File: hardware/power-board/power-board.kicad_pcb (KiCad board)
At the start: 2 copper layers, 197 x 65 mm, 25 parts, among them J1 SW_SPST, J2 Main Board, J3 DMX512 Out Jack, J4 DMX512, K1 SPST-NO, K2 SPST-NO, P1 IEC320-C14, P2 IEC320-C13, P3 IEC320-C13, U1 NUD3112DMT1G, U2 MAX3075E

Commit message: Updated PCB layout, still refining things
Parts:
- added LOGO: G***, lib_fp:Dektronics-logo, F.Cu at (94.0, 96.5)
- moved J2 58.4 mm to (156.0, 99.8)
- moved U1 37.9 mm to (142.2, 97.8)
- moved C1 23.1 mm to (209.6, 99.6), turned to -90 degrees
- moved NT1 15.0 mm to (220.0, 100.0), turned to 180 degrees
- moved D1 8.89 mm to (193.5, 99.6), turned to -90 degrees
- moved C2 8.13 mm to (201.9, 99.6), turned to -90 degrees
- moved U2 6.95 mm to (52.5, 76.5)
- moved C3 6.90 mm to (48.5, 72.9)
- moved TP1 6.16 mm to (175.5, 96.1)
- moved R1 4.83 mm to (52.5, 68.8)
- moved J4 4.39 mm to (52.0, 101.6)
- moved TP2 4.08 mm to (175.5, 102.2)
- moved F2 3.25 mm to (145.0, 83.8)
- moved J1 1.00 mm to (161.0, 61.0)
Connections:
- C3 pad 2: GND -> GND1
- J3 pad 1: GND -> GND1
- J4 pad 6: GND -> GND1
- U2 pad 5: GND -> GND1
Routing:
- net +12V: track 101.2 -> 198.0 mm
- net Net-(K2-Pad1): track 0.00 -> 62.3 mm
- net GND1: track 0.00 -> 55.5 mm, vias 0 -> 2
- net GND: track 162.6 -> 123.0 mm, vias 3 -> 2
- net /RELAY_ENLARGER: track 0.00 -> 28.9 mm, vias 0 -> 2
- net /RELAY_SAFELIGHT: track 0.00 -> 21.3 mm, vias 0 -> 2
- net Net-(K1-Pad1): track 0.00 -> 17.0 mm
- net NEUT: track 157.2 -> 166.8 mm
- net /RX: track 29.4 -> 20.6 mm
- net +3.3V: track 37.0 -> 28.3 mm
- net /RX_EN: track 29.3 -> 20.8 mm
- net /TX_EN: track 29.2 -> 20.9 mm
- net /TX: track 29.1 -> 21.0 mm
- net Net-(J1-Pad1): track 58.9 -> 65.8 mm
- net /RS-485+: track 11.9 -> 18.7 mm
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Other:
- board text added: "+12V"
- board text added: "+3.3V"
- board text added: "DMX512"
- board text added: "ENLG"
- board text added: "GND"
- board text added: "Printalyzer Enlarging Timer Power Input Board"
- board text added: "Rev: ${REVISION} ${ISSUE_DATE}"
- board text added: "SFLT"

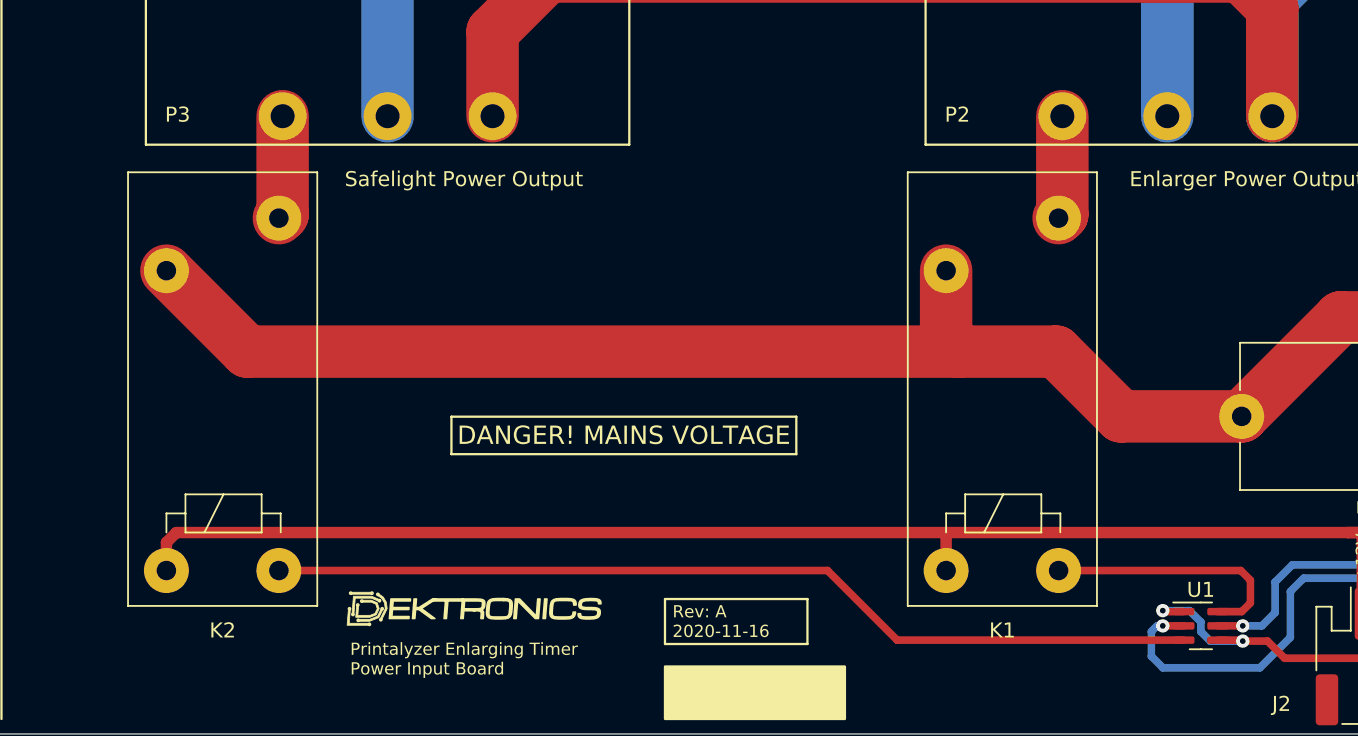
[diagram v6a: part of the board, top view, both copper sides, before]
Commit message: Symbol and PCB layout tweaks
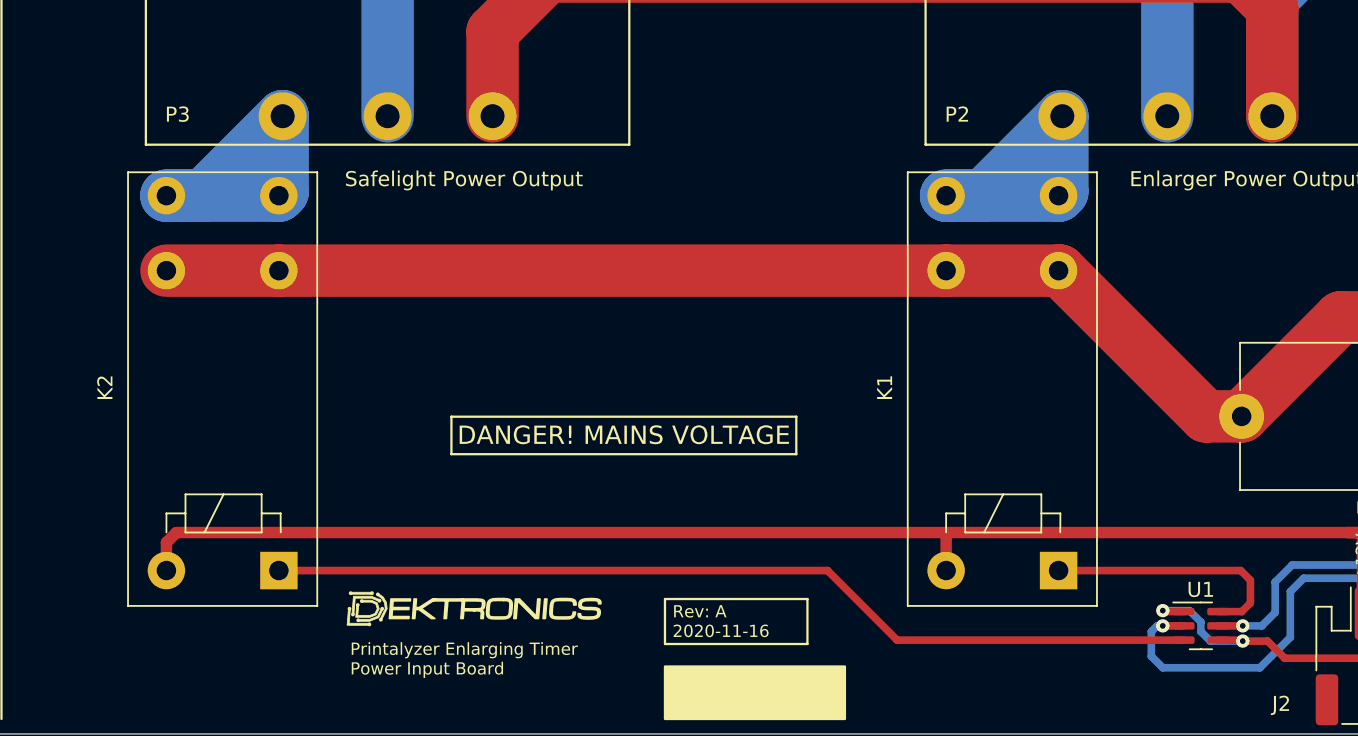
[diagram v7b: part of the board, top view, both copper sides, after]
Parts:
- K1, K2: footprint lib_fp:Relay_SPST_Omron_G2RL-1A -> lib_fp:Relay_SPST_Omron_G2RL-1A-E
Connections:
- K1 pad 3: Net-(K1-Pad3) -> LINE
- K1 pad 4: LINE -> /ENLG_AC_L
- K1 pad 5: +12V -> /ENLG_AC_L
- K2 pad 3: Net-(K2-Pad3) -> LINE
- K2 pad 4: LINE -> /SFLT_AC_L
- K2 pad 5: +12V -> /SFLT_AC_L
- P2 pad 1: Net-(K1-Pad3) -> /ENLG_AC_L
- P3 pad 1: Net-(K2-Pad3) -> /SFLT_AC_L
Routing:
- net /SFLT_AC_L: track 0.00 -> 22.8 mm
- net /ENLG_AC_L: track 0.00 -> 22.8 mm
- net Net-(K2-Pad3): track 6.90 -> 0.00 mm
- net Net-(K1-Pad3): track 6.90 -> 0.00 mm
- net LINE: track 115.4 -> 109.7 mm
